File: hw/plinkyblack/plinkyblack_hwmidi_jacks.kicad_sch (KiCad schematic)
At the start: 300 parts, among them J1 AudioJack2_SwitchT, J10 AudioJack2_SwitchT, J11 AudioJack2_SwitchT, J12 Conn_02x08_Odd_Even, J13 Conn_02x08_Odd_Even, J14 AudioJack2_SwitchT, J15 AudioJack2_SwitchT, J16 AudioJack2_SwitchT, J17 AudioJack2_SwitchT, J2 AudioJack2_SwitchT, J20 oled0.91, J22 AudioJack2_SwitchT, J23 AudioJack2_SwitchT, J25 Conn_01x16_Female, J28 PJ313, J29 PJ313, J3 AudioJack2_SwitchT, J30 PJ313, J31 PJ313, J32 PJ313, J33 PJ313, J4 AudioJack2_SwitchT, J5 SWD header, J6 AudioJack2_SwitchT, J7 AudioJack2_SwitchT, J8 AudioJack2_SwitchT, J9 AudioJack2_SwitchT, Q1 MMBT3904, U1 HCPL-0631-500E, U1 MCP6002-xSN, U10 TL072, U11 TL072, U12 W25Q32JVSS, U13 TPS61040DBV, U14 W25Q32JVSS, U15 WE-TVS-824001, U16 TL072, U17 LIS2DH12, U18 TL072, U19 TYPE-C-31-M-14, U2 LM1117-3.3, U20 TYPE-C-31-M-14, U22 PI3USB102EZLE, U23 WE-TVS-824001, U3 LM1117-3.3, U4 STM32L476VGT6, U5 TL072, U6 WM8758B, U7 TL072, U8 MCP6002-xSN, U9 MCP6002-xSN, Y1 Crystal_GND24

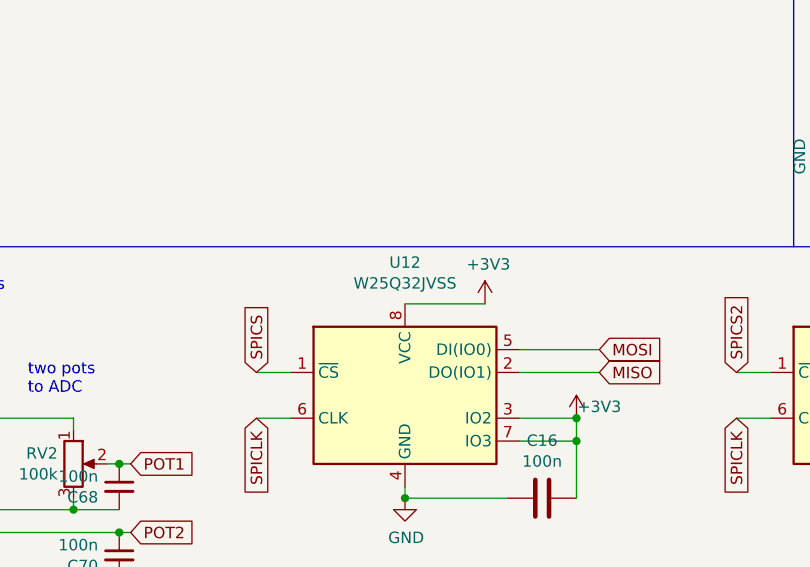
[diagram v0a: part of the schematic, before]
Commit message: Replaced W25Q32JVSS with W25Q128JVSIQ for the flash chip
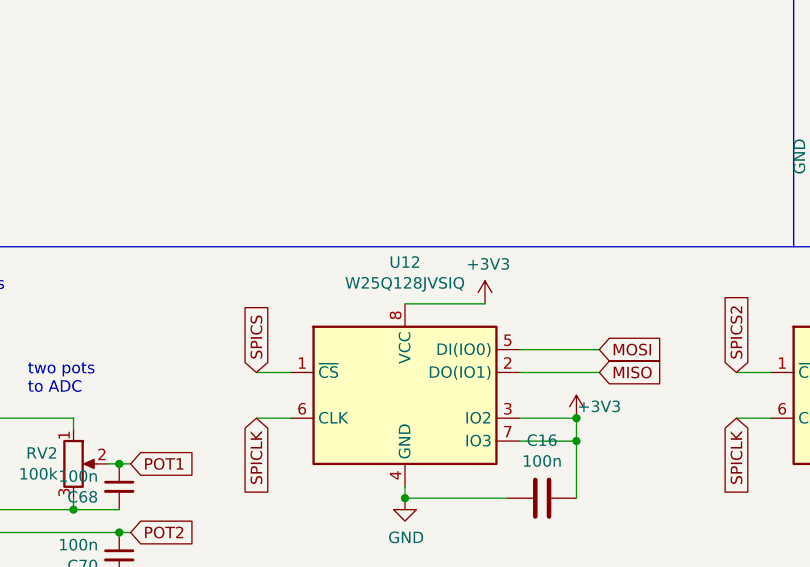
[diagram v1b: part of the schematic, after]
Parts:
- U12: value W25Q32JVSS -> W25Q128JVSIQ
